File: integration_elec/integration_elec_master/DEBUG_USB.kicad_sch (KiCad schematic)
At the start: 11 parts, among them J2 USB_C_Receptacle_USB2.0_16P, J7 CONN_02X05, U1 USBLC6-2SC6

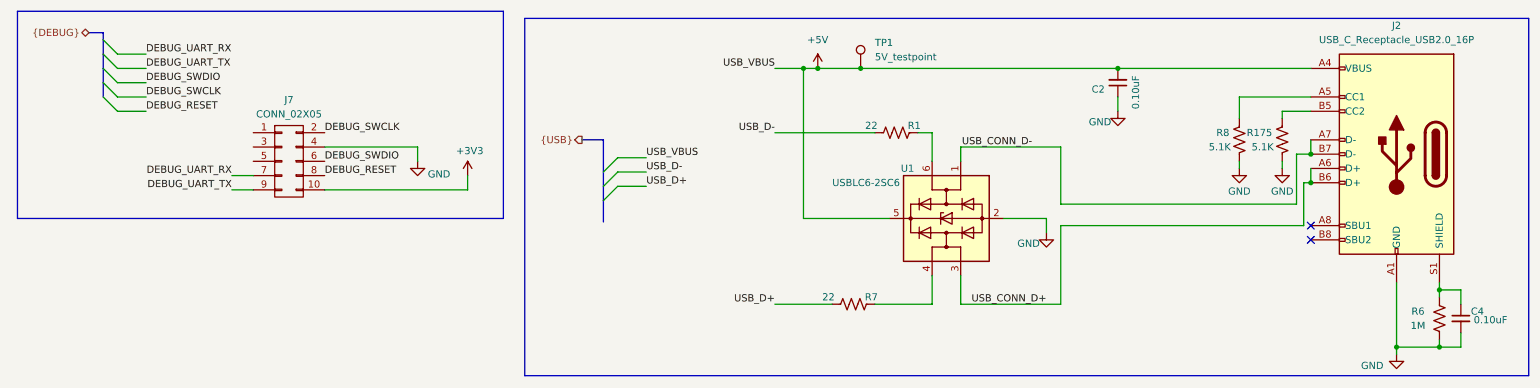
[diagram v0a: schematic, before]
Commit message: Added footprint, symbol, 3D model for joystick. Added schematic for Joystick and comments
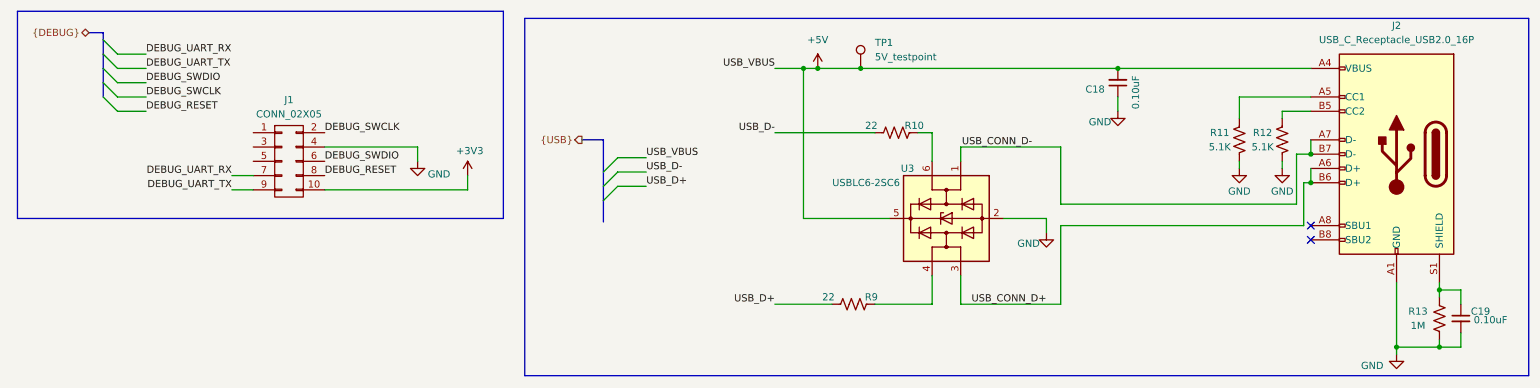
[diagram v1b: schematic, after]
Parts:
- renumbered C2 to C18, C4 to C19, J7 to J1, R1 to R10, R8 to R11, R175 to R12, R6 to R13, R7 to R9, U1 to U3
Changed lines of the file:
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@@
 		(on_board yes)
 		(dnp no)
-		(property "Reference" "R7"
+		(property "Reference" "R9"
 			(at 165.735 64.77 90)
 			(effects
@@
 			(project "integration_elec_master"
 				(path "/7d904e0d-c2b1-4329-81a9-fc34d181a4fe/ef54b424-e17d-48b3-87ed-158617f93c7a"
-					(reference "R7")
+					(reference "R9")
 					(unit 1)
 				)
@@
 		(on_board yes)
 		(dnp no)
-		(property "Reference" "R6"
+		(property "Reference" "R13"
 			(at 262.89 67.31 0)
 			(effects
@@
 			(project "integration_elec_master"
 				(path "/7d904e0d-c2b1-4329-81a9-fc34d181a4fe/ef54b424-e17d-48b3-87ed-158617f93c7a"
-					(reference "R6")
+					(reference "R13")
 					(unit 1)
 				)
@@
 		(on_board yes)
 		(dnp no)
-		(property "Reference" "R1"
+		(property "Reference" "R10"
 			(at 173.355 34.29 90)
 			(effects
@@
 			(project "integration_elec_master"
 				(path "/7d904e0d-c2b1-4329-81a9-fc34d181a4fe/ef54b424-e17d-48b3-87ed-158617f93c7a"
-					(reference "R1")
+					(reference "R10")
 					(unit 1)
 				)
@@
 		(on_board yes)
 		(dnp no)
-		(property "Reference" "#PWR183"
+		(property "Reference" "#PWR027"
 			(at 238.76 48.26 0)
 			(effects
@@
 			(project "integration_elec_master"
 				(path "/7d904e0d-c2b1-4329-81a9-fc34d181a4fe/ef54b424-e17d-48b3-87ed-158617f93c7a"
-					(reference "#PWR183")
+					(reference "#PWR027")
 					(unit 1)
 				)
@@
 		(dnp no)
 		(fields_autoplaced yes)
-		(property "Reference" "J7"
+		(property "Reference" "J1"
 			(at 62.23 29.718 0)
 			(effects
@@
 			(project "integration_elec_master"
 				(path "/7d904e0d-c2b1-4329-81a9-fc34d181a4fe/ef54b424-e17d-48b3-87ed-158617f93c7a"
-					(reference "J7")
+					(reference "J1")
 					(unit 1)
 				)
@@
 		(on_board yes)
 		(dnp no)
-		(property "Reference" "R175"
+		(property "Reference" "R12"
 			(at 236.982 35.56 0)
 			(effects
@@
 			(project "integration_elec_master"
 				(path "/7d904e0d-c2b1-4329-81a9-fc34d181a4fe/ef54b424-e17d-48b3-87ed-158617f93c7a"
-					(reference "R175")
+					(reference "R12")
 					(unit 1)
 				)
@@
 		(on_board yes)
 		(dnp no)
-		(property "Reference" "#PWR16"
+		(property "Reference" "#PWR022"
 			(at 93.98 46.99 0)
 			(effects
@@
 			(project "integration_elec_master"
 				(path "/7d904e0d-c2b1-4329-81a9-fc34d181a4fe/ef54b424-e17d-48b3-87ed-158617f93c7a"
-					(reference "#PWR16")
+					(reference "#PWR022")
 					(unit 1)
 				)
@@
 		(on_board yes)
 		(dnp no)
-		(property "Reference" "#PWR185"
+		(property "Reference" "#PWR026"
 			(at 231.14 48.26 0)
 			(effects
@@
 			(project "integration_elec_master"
 				(path "/7d904e0d-c2b1-4329-81a9-fc34d181a4fe/ef54b424-e17d-48b3-87ed-158617f93c7a"
-					(reference "#PWR185")
+					(reference "#PWR026")
 					(unit 1)
 				)
@@
 		(on_board yes)
 		(dnp no)
-		(property "Reference" "R8"
+		(property "Reference" "R11"
 			(at 229.362 35.56 0)
 			(effects
@@
 			(project "integration_elec_master"
 				(path "/7d904e0d-c2b1-4329-81a9-fc34d181a4fe/ef54b424-e17d-48b3-87ed-158617f93c7a"
-					(reference "R8")
+					(reference "R11")
 					(unit 1)
 				)
@@
 		(on_board yes)
 		(dnp no)
-		(property "Reference" "#PWR17"
+		(property "Reference" "#PWR028"
 			(at 259.08 81.28 0)
 			(effects
@@
 			(project "integration_elec_master"
 				(path "/7d904e0d-c2b1-4329-81a9-fc34d181a4fe/ef54b424-e17d-48b3-87ed-158617f93c7a"
-					(reference "#PWR17")
+					(reference "#PWR028")
 					(unit 1)
 				)
@@
 		(on_board yes)
 		(dnp no)
-		(property "Reference" "#PWR11"
+		(property "Reference" "#PWR024"
 			(at 196.85 59.69 0)
 			(effects
@@
 			(project "integration_elec_master"
 				(path "/7d904e0d-c2b1-4329-81a9-fc34d181a4fe/ef54b424-e17d-48b3-87ed-158617f93c7a"
-					(reference "#PWR11")
+					(reference "#PWR024")
 					(unit 1)
 				)
@@
 		(on_board yes)
 		(dnp no)
-		(property "Reference" "#PWR15"
+		(property "Reference" "#PWR021"
 			(at 85.09 46.99 0)
 			(effects
@@
 			(project "integration_elec_master"
 				(path "/7d904e0d-c2b1-4329-81a9-fc34d181a4fe/ef54b424-e17d-48b3-87ed-158617f93c7a"
-					(reference "#PWR15")
+					(reference "#PWR021")
 					(unit 1)
 				)
@@
 		(on_board yes)
 		(dnp no)
-		(property "Reference" "C4"
+		(property "Reference" "C19"
 			(at 272.288 67.31 0)
 			(effects
@@
 			(project "integration_elec_master"
 				(path "/7d904e0d-c2b1-4329-81a9-fc34d181a4fe/ef54b424-e17d-48b3-87ed-158617f93c7a"
-					(reference "C4")
+					(reference "C19")
 					(unit 1)
 				)
@@
 		(on_board yes)
 		(dnp no)
-		(property "Reference" "#PWR9"
+		(property "Reference" "#PWR025"
 			(at 209.55 38.1 0)
 			(effects
@@
 			(project "integration_elec_master"
 				(path "/7d904e0d-c2b1-4329-81a9-fc34d181a4fe/ef54b424-e17d-48b3-87ed-158617f93c7a"
-					(reference "#PWR9")
+					(reference "#PWR025")
 					(unit 1)
 				)
@@
 		(on_board yes)
 		(dnp no)
-		(property "Reference" "C2"
+		(property "Reference" "C18"
 			(at 207.2132 27.8384 0)
 			(effects
@@
 			(project "integration_elec_master"
 				(path "/7d904e0d-c2b1-4329-81a9-fc34d181a4fe/ef54b424-e17d-48b3-87ed-158617f93c7a"
-					(reference "C2")
+					(reference "C18")
 					(unit 1)
 				)
@@
 		(on_board yes)
 		(dnp no)
-		(property "Reference" "U1"
+		(property "Reference" "U3"
 			(at 173.355 41.91 90)
 			(effects
@@
 			(project "integration_elec_master"
 				(path "/7d904e0d-c2b1-4329-81a9-fc34d181a4fe/ef54b424-e17d-48b3-87ed-158617f93c7a"
-					(reference "U1")
+					(reference "U3")
 					(unit 1)
 				)
@@
 		(dnp no)
 		(fields_autoplaced yes)
-		(property "Reference" "#PWR01"
+		(property "Reference" "#PWR023"
 			(at 156.21 27.94 0)
 			(effects
@@
 			(project ""
 				(path "/7d904e0d-c2b1-4329-81a9-fc34d181a4fe/ef54b424-e17d-48b3-87ed-158617f93c7a"
-					(reference "#PWR01")
+					(reference "#PWR023")
 					(unit 1)
 				)

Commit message: Added plein de footprint
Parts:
- J1: footprint Esteban11:CONN_CNC_10_pins -> JOYSTICK:CONN_3220-10-0100-00_CNC
- TP1: footprint (none) -> TestPoint:TestPoint_Plated_Hole_D2.0mm
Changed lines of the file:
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@@
 			)
 		)
-		(property "Footprint" ""
+		(property "Footprint" "TestPoint:TestPoint_Plated_Hole_D2.0mm"
 			(at 168.91 24.13 0)
 			(effects
@@
 			)
 		)
-		(property "Footprint" "Esteban11:CONN_CNC_10_pins"
+		(property "Footprint" "JOYSTICK:CONN_3220-10-0100-00_CNC"
 			(at 62.23 71.12 0)
 			(effects

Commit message: KAH - Fini schematic attente de review + correction BUS
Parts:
- renumbered R9 to R11, R10 to R12, R11 to R13, R12 to R14, R13 to R15
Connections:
- net DEBUG_NJTRST: now reaches J1.1 (P1)
- net DEBUG_SWO_TDI: now reaches J1.3 (P3)
- net DEBUG_SWO_TDO: now reaches J1.5 (P5)

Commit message: KAH - added the part # for some pieces. MISSING R NC and USB-C conn
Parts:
- R13, R14: DigiKey (none) -> 311-5.10KHRCT-ND
- TP1: now left out of the parts list
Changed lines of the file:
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@@
 		(unit 1)
 		(exclude_from_sim no)
-		(in_bom yes)
+		(in_bom no)
 		(on_board yes)
 		(dnp no)
@@
 			)
 		)
+		(property "DigiKey" "311-5.10KHRCT-ND"
+			(at 238.76 36.83 0)
+			(effects
+				(font
+					(size 1.27 1.27)
+				)
+				(hide yes)
+			)
+		)
 		(pin "1"
 		)
@@
 			(at 231.14 36.83 0)
 			(effects
+				(font
+					(size 1.27 1.27)
+				)
+				(hide yes)
+			)
+		)
+		(property "DigiKey" "311-5.10KHRCT-ND"
+			(at 231.14 36.83 0)
+			(effects
